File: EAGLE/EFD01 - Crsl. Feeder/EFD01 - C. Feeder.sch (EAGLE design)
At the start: 35 parts, among them J1 MOD TOOL, J2 SPI, J3 MOT, J4 FTDI, Q1 BSS138, Q2 16MHz, U1 SP3485, U2 TCST1030, U3 ATMEGA238, U4 DRV8825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

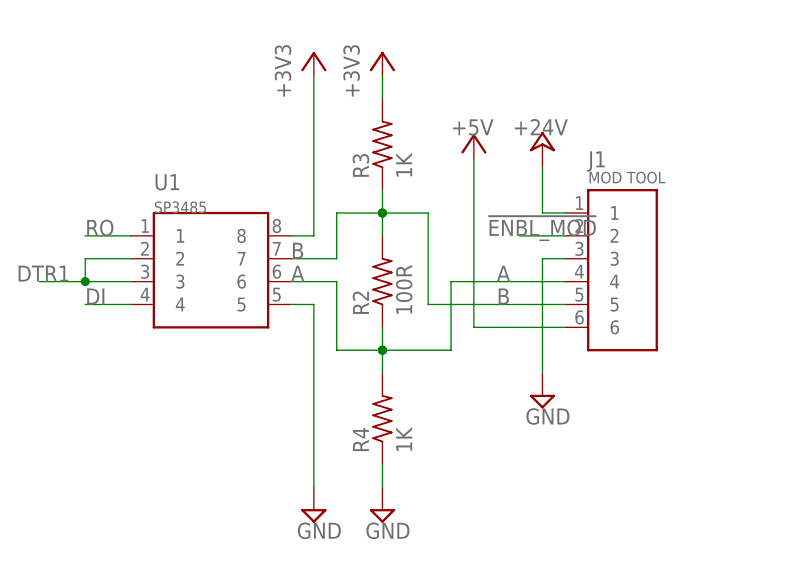
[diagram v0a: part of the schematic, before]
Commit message: BOMs finished, inventory sheet created.
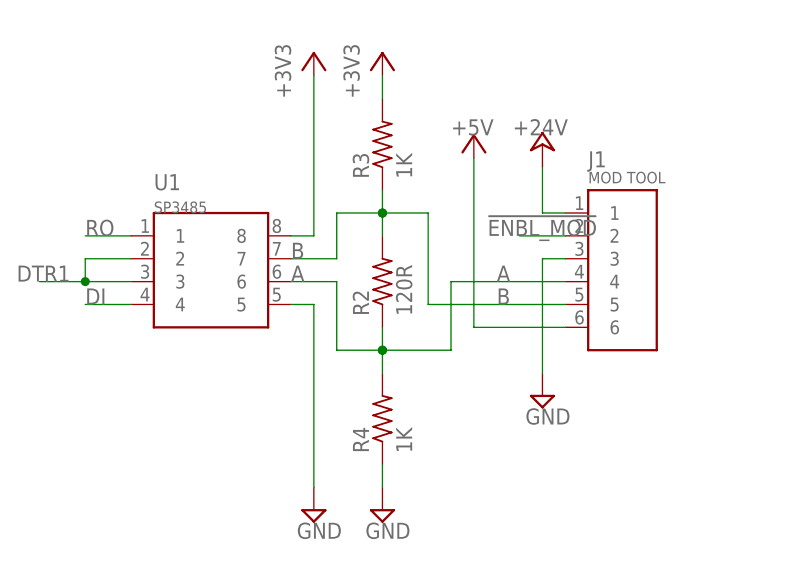
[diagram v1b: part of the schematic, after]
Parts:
- R2: value 100R -> 120R; device TinWhiskers:CPL-RES-0603-100-0.1W -> TinWhiskers:CPL-RES-0603-120-0.1W
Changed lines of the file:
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@@
 <part name="P+1" library="supply1" deviceset="+24V" device=""/>
 <part name="P+2" library="supply1" deviceset="+5V" device=""/>
-<part name="R2" library="TinWhiskers" deviceset="CPL-RES-0603-100-0.1W" device="" value="100R">
+<part name="R2" library="TinWhiskers" deviceset="CPL-RES-0603-120-0.1W" device="" value="120R">
 <attribute name="PARTNO" value="RC0603FR-07100RL"/>
 </part>

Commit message: Updated some of the attributes on schematics which contained incorrect part numbers. Similarly adjusted BOMs and inventory/PO form to reflect these changes.
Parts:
- R2: PARTNO RC0603FR-07100RL -> RC0603FR-07120RL
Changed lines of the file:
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@@
 <part name="P+2" library="supply1" deviceset="+5V" device=""/>
 <part name="R2" library="TinWhiskers" deviceset="CPL-RES-0603-120-0.1W" device="" value="120R">
-<attribute name="PARTNO" value="RC0603FR-07100RL"/>
+<attribute name="PARTNO" value="RC0603FR-07120RL"/>
 </part>
 <part name="VR1" library="TinWhiskers" deviceset="CPL-REG-LIN-3.3V-0.1A" device="" value="TC1015-3.3VCT713">

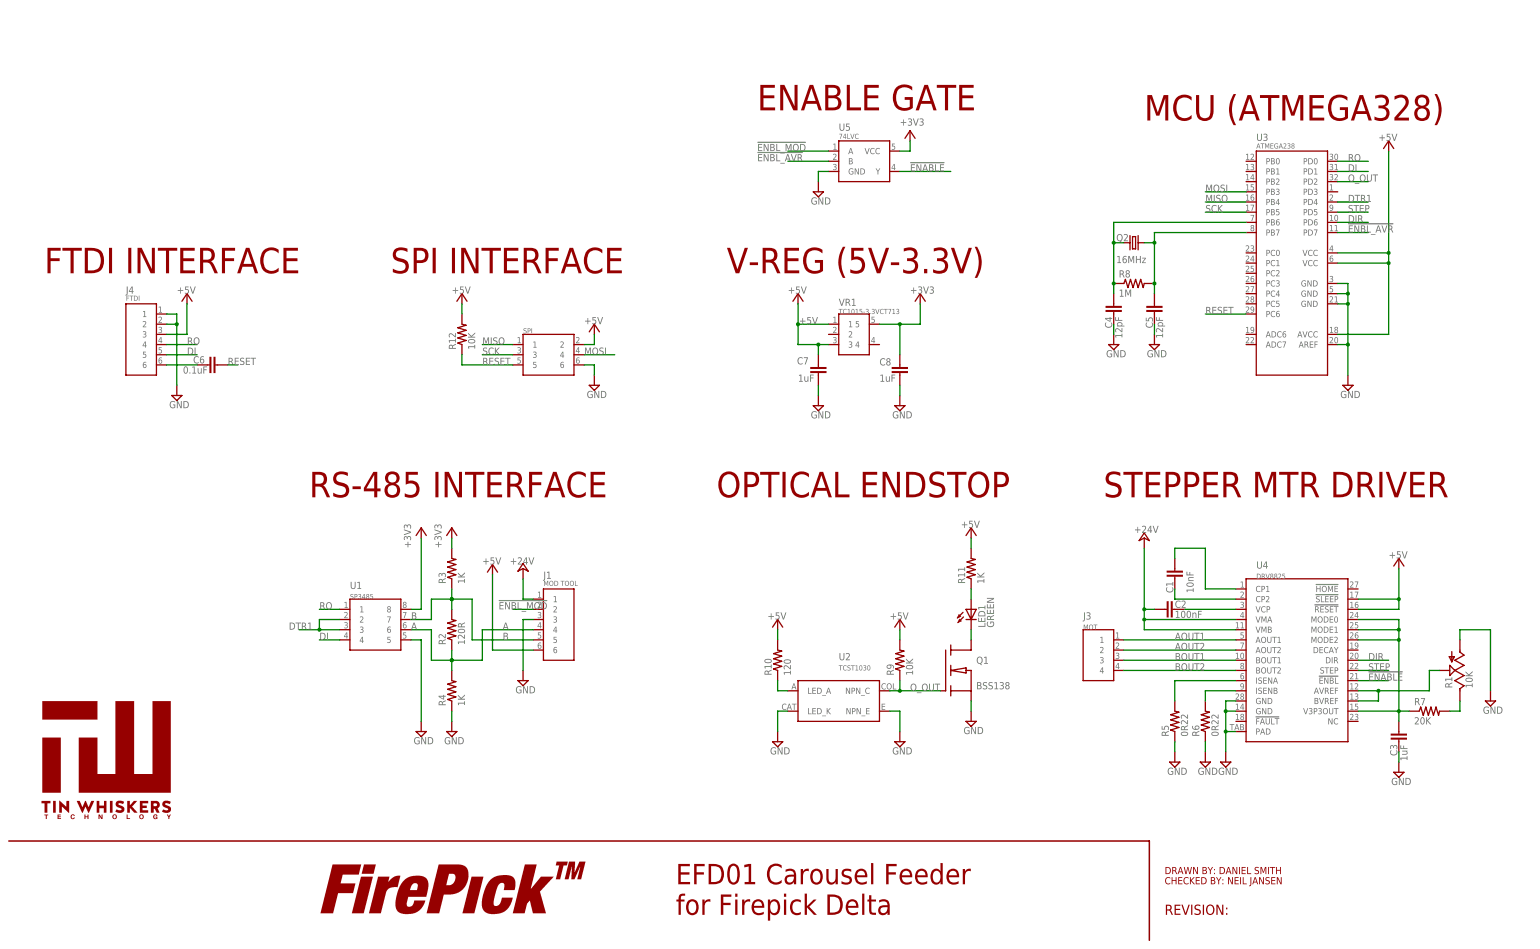
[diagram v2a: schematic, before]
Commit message: Added decoupling caps to EFD01, ECAM02, rearranged parts for better fit, increased power trace width, updated BOM and database.
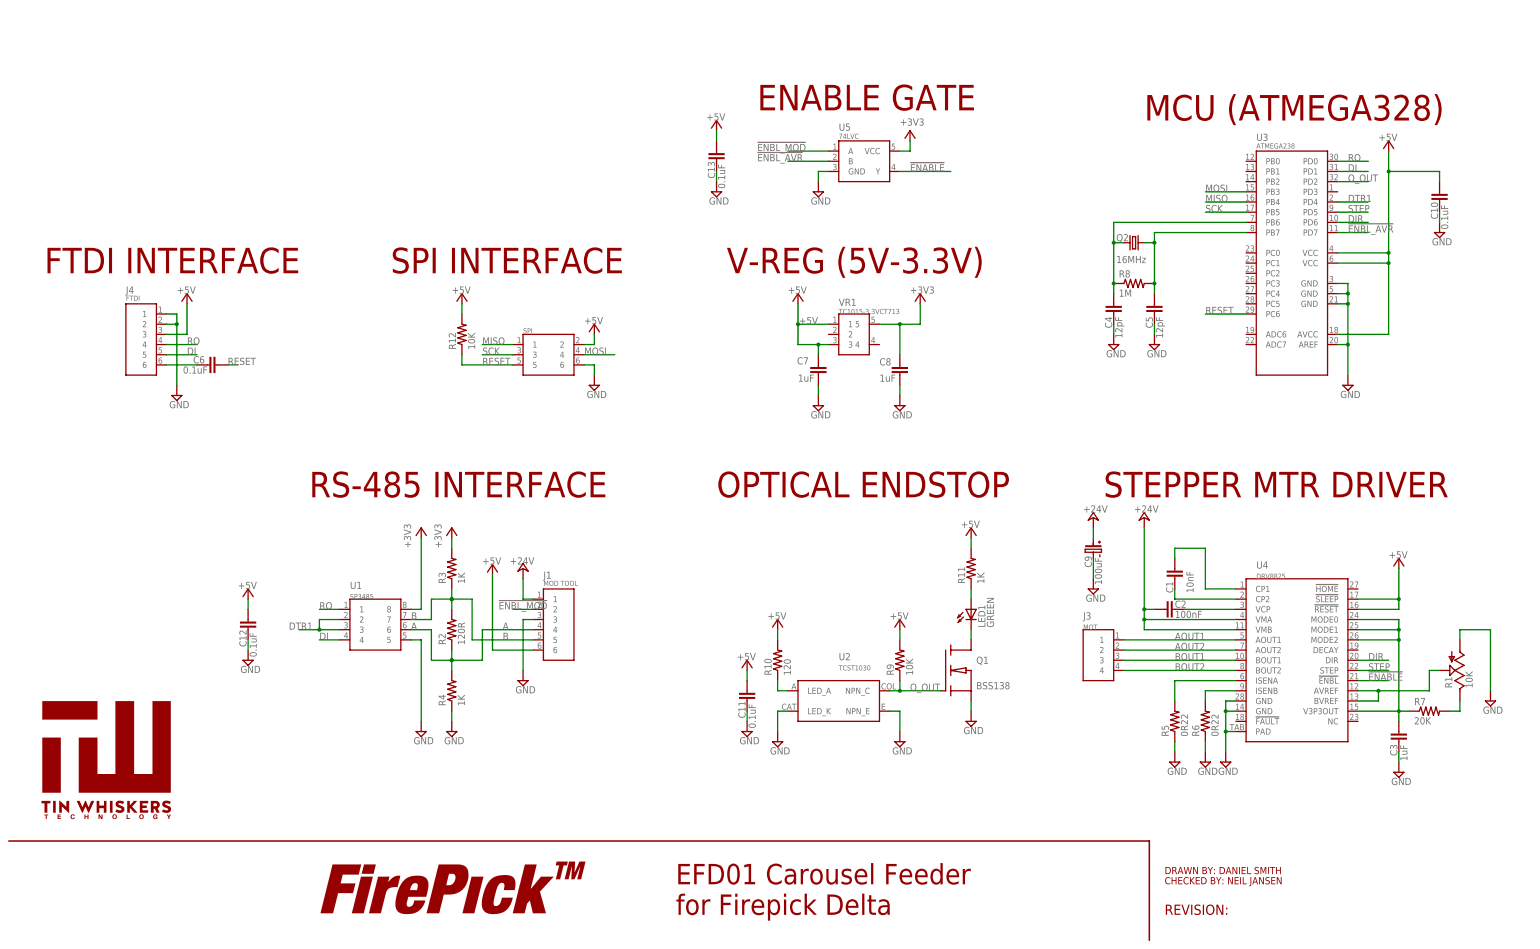
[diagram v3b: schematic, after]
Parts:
- added C10, C11, C12, C13: 0.1uF, TinWhiskers:CPL-CAP-X7R-0603-0.1UF-35V
- added C9: 100uF, TinWhiskers:CPL-CAP-ALU-SMD-100UF-50V
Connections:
- net +24V: now also C9.POS
- net +5V: now also C10.2, C11.2, C12.2, C13.2
- net GND: now also C10.1, C11.1, C12.1, C13.1, C9.NEG
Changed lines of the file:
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@@
 <attribute name="PARTNO" value="*"/>
 </part>
+<part name="C9" library="TinWhiskers" deviceset="CPL-CAP-ALU-SMD-100UF-50V" device="" value="100uF"/>
+<part name="SUPPLY11" library="TinWhiskers" deviceset="GND" device=""/>
+<part name="P+13" library="supply1" deviceset="+24V" device=""/>
+<part name="C10" library="TinWhiskers" deviceset="CPL-CAP-X7R-0603-0.1UF-35V" device="" value="0.1uF"/>
+<part name="SUPPLY19" library="TinWhiskers" deviceset="GND" device=""/>
+<part name="C11" library="TinWhiskers" deviceset="CPL-CAP-X7R-0603-0.1UF-35V" device="" value="0.1uF"/>
+<part name="P+14" library="supply1" deviceset="+5V" device=""/>
+<part name="SUPPLY20" library="TinWhiskers" deviceset="GND" device=""/>
+<part name="C12" library="TinWhiskers" deviceset="CPL-CAP-X7R-0603-0.1UF-35V" device="" value="0.1uF"/>
+<part name="P+15" library="supply1" deviceset="+5V" device=""/>
+<part name="SUPPLY21" library="TinWhiskers" deviceset="GND" device=""/>
+<part name="C13" library="TinWhiskers" deviceset="CPL-CAP-X7R-0603-0.1UF-35V" device="" value="0.1uF"/>
+<part name="P+16" library="supply1" deviceset="+5V" device=""/>
+<part name="SUPPLY24" library="TinWhiskers" deviceset="GND" device=""/>
 </parts>
 <sheets>
@@
 <attribute name="PARTNO" x="294.64" y="86.36" size="2.54" layer="96" ratio="10" display="off"/>
 </instance>
-<instance part="P+5" gate="1" x="287.02" y="104.14" smashed="yes">
-<attribute name="VALUE" x="284.48" y="105.41" size="1.778" layer="96"/>
+<instance part="P+5" gate="1" x="287.02" y="109.22" smashed="yes">
+<attribute name="VALUE" x="284.48" y="110.49" size="1.778" layer="96"/>
 </instance>
 <instance part="SUPPLY5" gate="GND" x="307.34" y="48.26"/>
@@
 <attribute name="PARTNO" x="10.16" y="33.02" size="1.778" layer="96" display="off"/>
 </instance>
+<instance part="C9" gate="G$1" x="274.32" y="101.6" smashed="yes" rot="R270">
+<attribute name="NAME" x="273.939" y="96.774" size="1.778" layer="95" rot="R90"/>
+<attribute name="VALUE" x="276.479" y="92.456" size="1.778" layer="96" rot="R90"/>
+</instance>
+<instance part="SUPPLY11" gate="GND" x="274.32" y="91.44"/>
+<instance part="P+13" gate="1" x="274.32" y="109.22" smashed="yes">
+<attribute name="VALUE" x="271.78" y="110.49" size="1.778" layer="96"/>
+</instance>
+<instance part="C10" gate="G$1" x="360.68" y="190.5" smashed="yes" rot="R90">
+<attribute name="NAME" x="360.299" y="183.642" size="1.778" layer="95" rot="R90"/>
+<attribute name="VALUE" x="362.839" y="181.102" size="1.778" layer="96" rot="R90"/>
+</instance>
+<instance part="SUPPLY19" gate="GND" x="360.68" y="180.34"/>
+<instance part="C11" gate="G$1" x="187.96" y="66.04" smashed="yes" rot="R90">
+<attribute name="NAME" x="187.579" y="59.182" size="1.778" layer="95" rot="R90"/>
+<attribute name="VALUE" x="190.119" y="56.642" size="1.778" layer="96" rot="R90"/>
+</instance>
+<instance part="P+14" gate="1" x="187.96" y="73.66" smashed="yes">
+<attribute name="VALUE" x="185.42" y="73.66" size="1.778" layer="96"/>
+</instance>
+<instance part="SUPPLY20" gate="GND" x="187.96" y="55.88"/>
+<instance part="C12" gate="G$1" x="63.5" y="83.82" smashed="yes" rot="R90">
+<attribute name="NAME" x="63.119" y="76.962" size="1.778" layer="95" rot="R90"/>
+<attribute name="VALUE" x="65.659" y="74.422" size="1.778" layer="96" rot="R90"/>
+</instance>
+<instance part="P+15" gate="1" x="63.5" y="91.44" smashed="yes">
+<attribute name="VALUE" x="60.96" y="91.44" size="1.778" layer="96"/>
+</instance>
+<instance part="SUPPLY21" gate="GND" x="63.5" y="73.66"/>
+<instance part="C13" gate="G$1" x="180.34" y="200.66" smashed="yes" rot="R90">
+<attribute name="NAME" x="179.959" y="193.802" size="1.778" layer="95" rot="R90"/>
+<attribute name="VALUE" x="182.499" y="191.262" size="1.778" layer="96" rot="R90"/>
+</instance>
+<instance part="P+16" gate="1" x="180.34" y="208.28" smashed="yes">
+<attribute name="VALUE" x="177.8" y="208.28" size="1.778" layer="96"/>
+</instance>
+<instance part="SUPPLY24" gate="GND" x="180.34" y="190.5"/>
 </instances>
 <busses>
@@
 <pinref part="SUPPLY4" gate="GND" pin="GND"/>
 </segment>
+<segment>
+<pinref part="C9" gate="G$1" pin="NEG"/>
+<pinref part="SUPPLY11" gate="GND" pin="GND"/>
+<wire x1="274.32" y1="99.06" x2="274.32" y2="93.98" width="0.1524" layer="91"/>
+</segment>
+<segment>
+<pinref part="C10" gate="G$1" pin="1"/>
+<pinref part="SUPPLY19" gate="GND" pin="GND"/>
+<wire x1="360.68" y1="185.42" x2="360.68" y2="182.88" width="0.1524" layer="91"/>
+</segment>
+<segment>
+<pinref part="C11" gate="G$1" pin="1"/>
+<pinref part="SUPPLY20" gate="GND" pin="GND"/>
+<wire x1="187.96" y1="60.96" x2="187.96" y2="58.42" width="0.1524" layer="91"/>
+</segment>
+<segment>
+<pinref part="C12" gate="G$1" pin="1"/>
+<pinref part="SUPPLY21" gate="GND" pin="GND"/>
+<wire x1="63.5" y1="78.74" x2="63.5" y2="76.2" width="0.1524" layer="91"/>
+</segment>
+<segment>
+<pinref part="C13" gate="G$1" pin="1"/>
+<pinref part="SUPPLY24" gate="GND" pin="GND"/>
+<wire x1="180.34" y1="195.58" x2="180.34" y2="193.04" width="0.1524" layer="91"/>
+</segment>
 </net>
 <net name="+24V" class="0">
@@
 <pinref part="C2" gate="C1" pin="1"/>
 <wire x1="289.56" y1="86.36" x2="287.02" y2="86.36" width="0.1524" layer="91"/>
-<wire x1="287.02" y1="86.36" x2="287.02" y2="101.6" width="0.1524" layer="91"/>
+<wire x1="287.02" y1="86.36" x2="287.02" y2="106.68" width="0.1524" layer="91"/>
 <junction x="287.02" y="86.36"/>
 <pinref part="P+5" gate="1" pin="+24V"/>
+</segment>
+<segment>
+<pinref part="C9" gate="G$1" pin="POS"/>
+<wire x1="274.32" y1="106.68" x2="274.32" y2="104.14" width="0.1524" layer="91"/>
+<pinref part="P+13" gate="1" pin="+24V"/>
 </segment>
 </net>
@@
 <pinref part="U3" gate="G$1" pin="VCC@4"/>
 <wire x1="335.28" y1="175.26" x2="347.98" y2="175.26" width="0.1524" layer="91"/>
-<wire x1="347.98" y1="175.26" x2="347.98" y2="200.66" width="0.1524" layer="91"/>
+<wire x1="347.98" y1="175.26" x2="347.98" y2="195.58" width="0.1524" layer="91"/>
+<wire x1="347.98" y1="195.58" x2="347.98" y2="200.66" width="0.1524" layer="91"/>
 <wire x1="347.98" y1="175.26" x2="347.98" y2="172.72" width="0.1524" layer="91"/>
 <junction x="347.98" y="175.26"/>
@@
 <wire x1="347.98" y1="154.94" x2="347.98" y2="172.72" width="0.1524" layer="91"/>
 <junction x="347.98" y="172.72"/>
+<pinref part="C10" gate="G$1" pin="2"/>
+<wire x1="347.98" y1="195.58" x2="360.68" y2="195.58" width="0.1524" layer="91"/>
+<wire x1="360.68" y1="195.58" x2="360.68" y2="193.04" width="0.1524" layer="91"/>
+<junction x="347.98" y="195.58"/>
 </segment>
 <segment>
@@
 <pinref part="P+11" gate="1" pin="+5V"/>
 </segment>
+<segment>
+<pinref part="P+14" gate="1" pin="+5V"/>
+<pinref part="C11" gate="G$1" pin="2"/>
+<wire x1="187.96" y1="71.12" x2="187.96" y2="68.58" width="0.1524" layer="91"/>
+</segment>
+<segment>
+<pinref part="P+15" gate="1" pin="+5V"/>
+<pinref part="C12" gate="G$1" pin="2"/>
+<wire x1="63.5" y1="88.9" x2="63.5" y2="86.36" width="0.1524" layer="91"/>
+</segment>
+<segment>
+<pinref part="P+16" gate="1" pin="+5V"/>
+<pinref part="C13" gate="G$1" pin="2"/>
+<wire x1="180.34" y1="205.74" x2="180.34" y2="203.2" width="0.1524" layer="91"/>
+</segment>
 </net>
